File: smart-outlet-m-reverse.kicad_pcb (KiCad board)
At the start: 2 copper layers, 60 x 33 mm, 61 parts, among them CN1 Conn_01x01, CN2 Conn_01x01, K1 HF32FV-16/5-HLTF(590), Q1 MMBT3904, SW1 B3F-3120, U1 OB2222M, U2 STK17-3.3, U3 CSE7759B

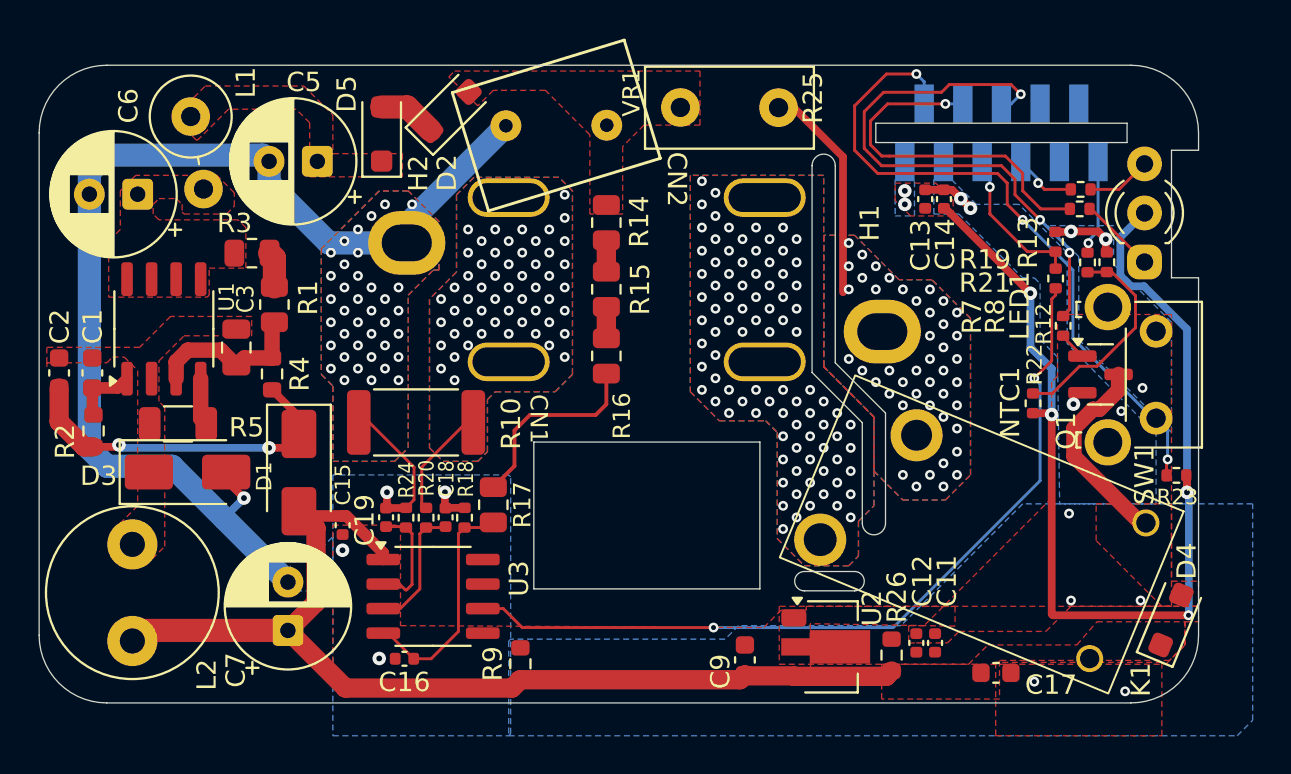
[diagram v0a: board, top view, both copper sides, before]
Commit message: Despite so many vias I realized I hadn't added some where they matter. Corrected.
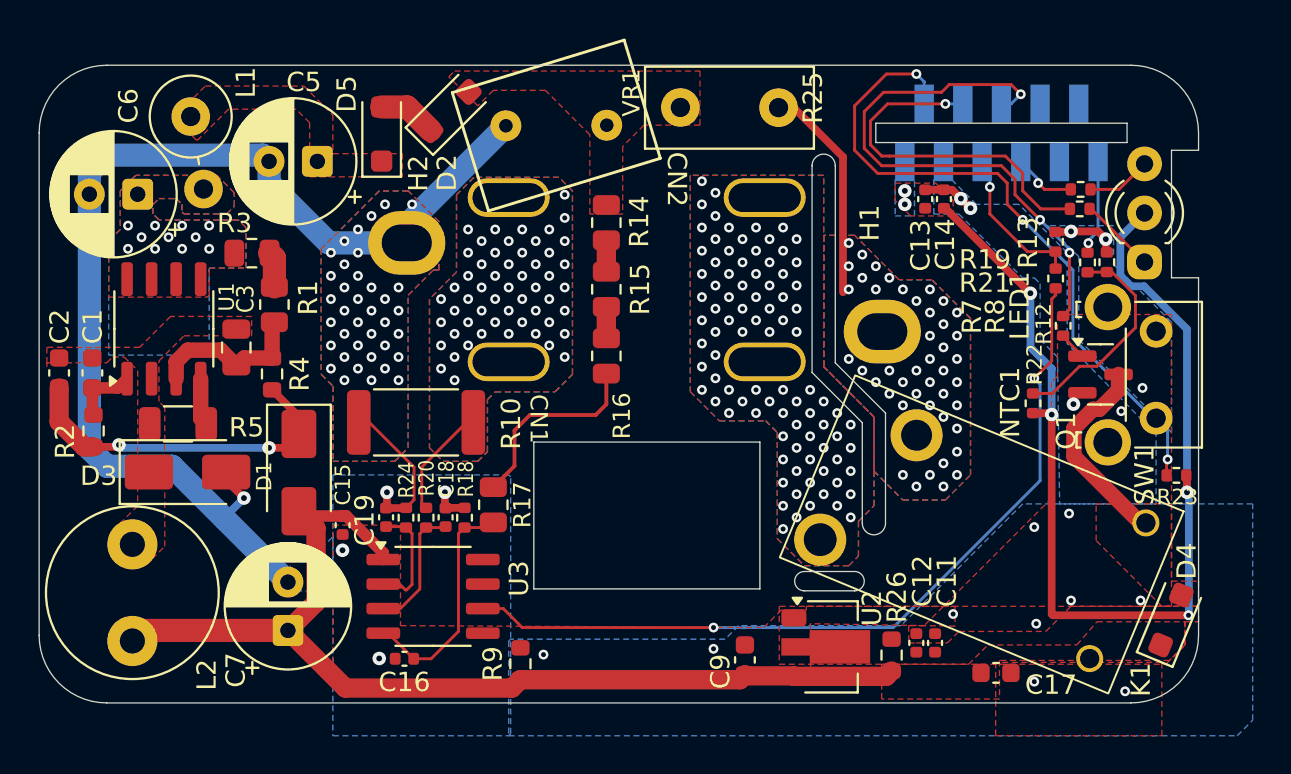
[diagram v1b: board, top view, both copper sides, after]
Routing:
- net NEUTRAL_SRC: vias 54 -> 59
- net /power supplies/HV_DC: vias 0 -> 11
- added copper zone on B.Cu, net /power supplies/HV_DC
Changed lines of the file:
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@@
 	)
 	(via
+		(at 173.5 107.4)
+		(size 0.508)
+		(drill 0.254)
+		(layers "F.Cu" "B.Cu")
+		(free yes)
+		(net 4)
+	)
+	(via
 		(at 139.6 114.2)
 		(size 0.7)
@@
 	)
 	(via
+		(at 148.1 114)
+		(size 0.508)
+		(drill 0.254)
+		(layers "F.Cu" "B.Cu")
+		(free yes)
+		(net 4)
+	)
+	(via
 		(at 139.2 95)
 		(size 0.508)
@@
 	)
 	(via
+		(at 173.6 112.4)
+		(size 0.508)
+		(drill 0.254)
+		(layers "F.Cu" "B.Cu")
+		(free yes)
+		(net 4)
+	)
+	(via
 		(at 138.5 96.8)
 		(size 0.508)
@@
 	)
 	(via
+		(at 156.9 113.7)
+		(size 0.508)
+		(drill 0.254)
+		(layers "F.Cu" "B.Cu")
+		(free yes)
+		(net 4)
+	)
+	(via
 		(at 139.9 96.8)
 		(size 0.508)
@@
 	)
 	(via
+		(at 169.3 111.9)
+		(size 0.508)
+		(drill 0.254)
+		(layers "F.Cu" "B.Cu")
+		(free yes)
+		(net 4)
+	)
+	(via
 		(at 175.525757 101.038372)
 		(size 0.7)
@@
 		(net 38)
 	)
+	(via
+		(at 126.6 93)
+		(size 0.508)
+		(drill 0.254)
+		(layers "F.Cu" "B.Cu")
+		(free yes)
+		(net 39)
+	)
+	(via
+		(at 128 93)
+		(size 0.508)
+		(drill 0.254)
+		(layers "F.Cu" "B.Cu")
+		(free yes)
+		(net 39)
+	)
+	(via
+		(at 126.6 91.8)
+		(size 0.508)
+		(drill 0.254)
+		(layers "F.Cu" "B.Cu")
+		(free yes)
+		(net 39)
+	)
+	(via
+		(at 129.4 91.8)
+		(size 0.508)
+		(drill 0.254)
+		(layers "F.Cu" "B.Cu")
+		(free yes)
+		(net 39)
+	)
+	(via
+		(at 130.8 91.8)
+		(size 0.508)
+		(drill 0.254)
+		(layers "F.Cu" "B.Cu")
+		(free yes)
+		(net 39)
+	)
+	(via
+		(at 127.3 92.4)
+		(size 0.508)
+		(drill 0.254)
+		(layers "F.Cu" "B.Cu")
+		(free yes)
+		(net 39)
+	)
+	(via
+		(at 129.4 93)
+		(size 0.508)
+		(drill 0.254)
+		(layers "F.Cu" "B.Cu")
+		(free yes)
+		(net 39)
+	)
+	(via
+		(at 128.7 92.4)
+		(size 0.508)
+		(drill 0.254)
+		(layers "F.Cu" "B.Cu")
+		(free yes)
+		(net 39)
+	)
+	(via
+		(at 128 91.8)
+		(size 0.508)
+		(drill 0.254)
+		(layers "F.Cu" "B.Cu")
+		(free yes)
+		(net 39)
+	)
+	(via
+		(at 130.1 92.4)
+		(size 0.508)
+		(drill 0.254)
+		(layers "F.Cu" "B.Cu")
+		(free yes)
+		(net 39)
+	)
+	(via
+		(at 130.8 93)
+		(size 0.508)
+		(drill 0.254)
+		(layers "F.Cu" "B.Cu")
+		(free yes)
+		(net 39)
+	)
 	(zone
 		(net 4)
@@
 			)
 		)
+	)
+	(zone
+		(net 39)
+		(net_name "/power supplies/HV_DC")
+		(layer "B.Cu")
+		(hatch edge 0.5)
+		(priority 10)
+		(connect_pads yes
+			(clearance 0.1524)
+		)
+		(min_thickness 0.1524)
+		(filled_areas_thickness no)
+		(fill yes
+			(thermal_gap 0.2)
+			(thermal_bridge_width 0.2)
+		)
+		(polygon
+			(pts
+				(xy 127 89.2) (xy 126.2 90) (xy 126.2 92) (xy 125.8 92.4) (xy 125.6 92.4) (xy 125.6 98.5) (xy 130.5 98.5)
+				(xy 130.8 98.2) (xy 130.8 94) (xy 132.7 94) (xy 132.7 91.9) (xy 132.3 91.5) (xy 128.2 91.5) (xy 127.9 91.2)
+				(xy 127.9 90.7) (xy 128.2 90.4) (xy 129.1 90.4) (xy 129.4 90.7) (xy 129.4 91.1) (xy 129.5 91.2)
+				(xy 131.7 91.2) (xy 132.1 90.8) (xy 132.1 90.1) (xy 131.2 89.2)
+			)
+		)

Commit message: Rearranged SMPS circuit. Added a lot of schematic comments. Moved RECT_AC line away from NEUTRAL_SRC (not enough). Updated README greatly. Added pictures. Added PDF schematic.
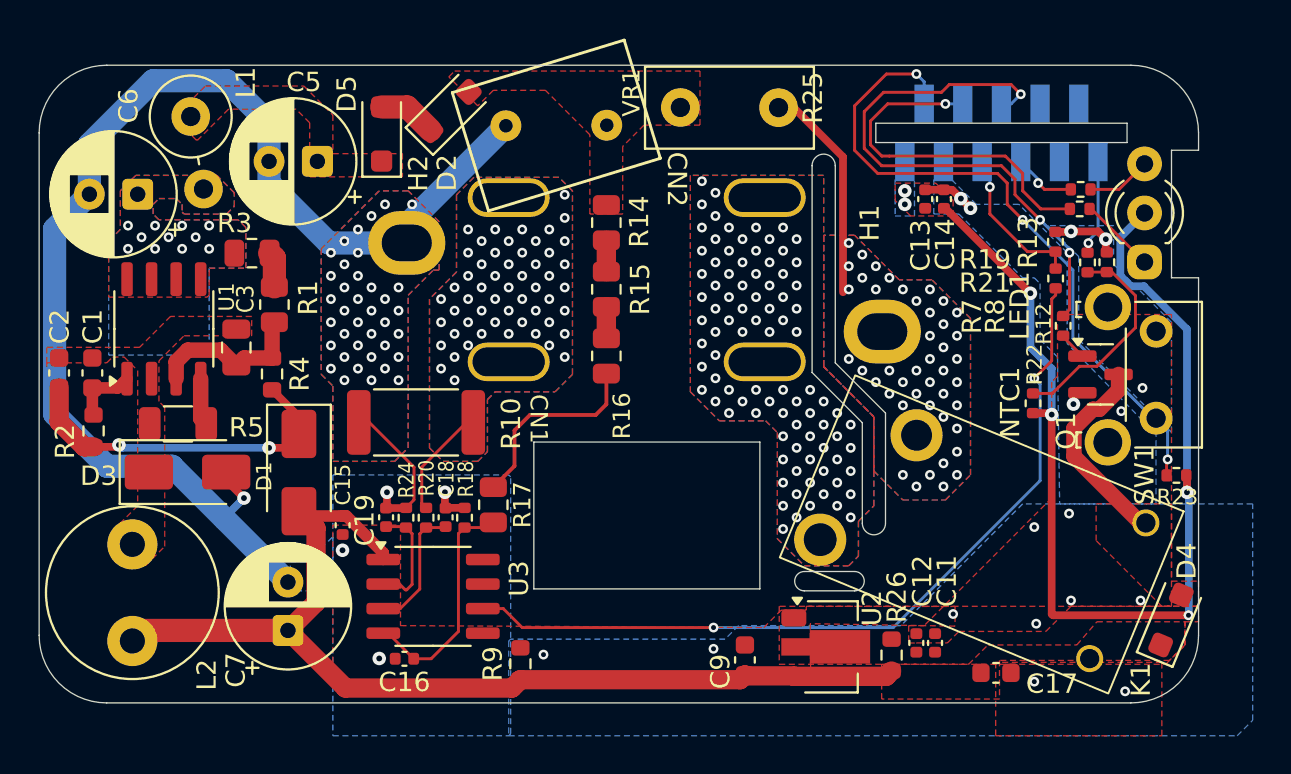
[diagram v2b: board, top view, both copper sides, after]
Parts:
- C11, C12, C13, C14, C17, C9: value 10µF -> 10µ
- C15: value 1µF -> 1µ
- C16, C18, C19: value 33nF -> 33n
- C3: value 4.7µF -> 4.7µ
- C5, C6: value 3.3uF -> 3.3u
- C7: value 470µF -> 470µ
- NTC1, R19, R8: value 10kΩ -> 10k
- R1, R3: value 1MΩ -> 1M
- R10: value 1mΩ -> 1m
- R12, R18, R20, R21, R24: value 1kΩ -> 1k
- R13: value 2kΩ -> 2k
- R14, R15, R16, R17: value 470kΩ -> 470k
- R2: value 0Ω -> 0
- R22, R9: value 1K -> 1k
- R23: value 1KΩ -> 1k
- R5: value 500mΩ -> 500m
- R7: value 100Ω -> 100
- VR1: value 07D-418K -> 07D-471K
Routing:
- net NEUTRAL_SRC: track 74.2 -> 80.9 mm
